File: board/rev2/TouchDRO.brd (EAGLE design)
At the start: 50.8 x 50.8 mm, 26 parts, among them U2 VREG_33, U3 VREG_5

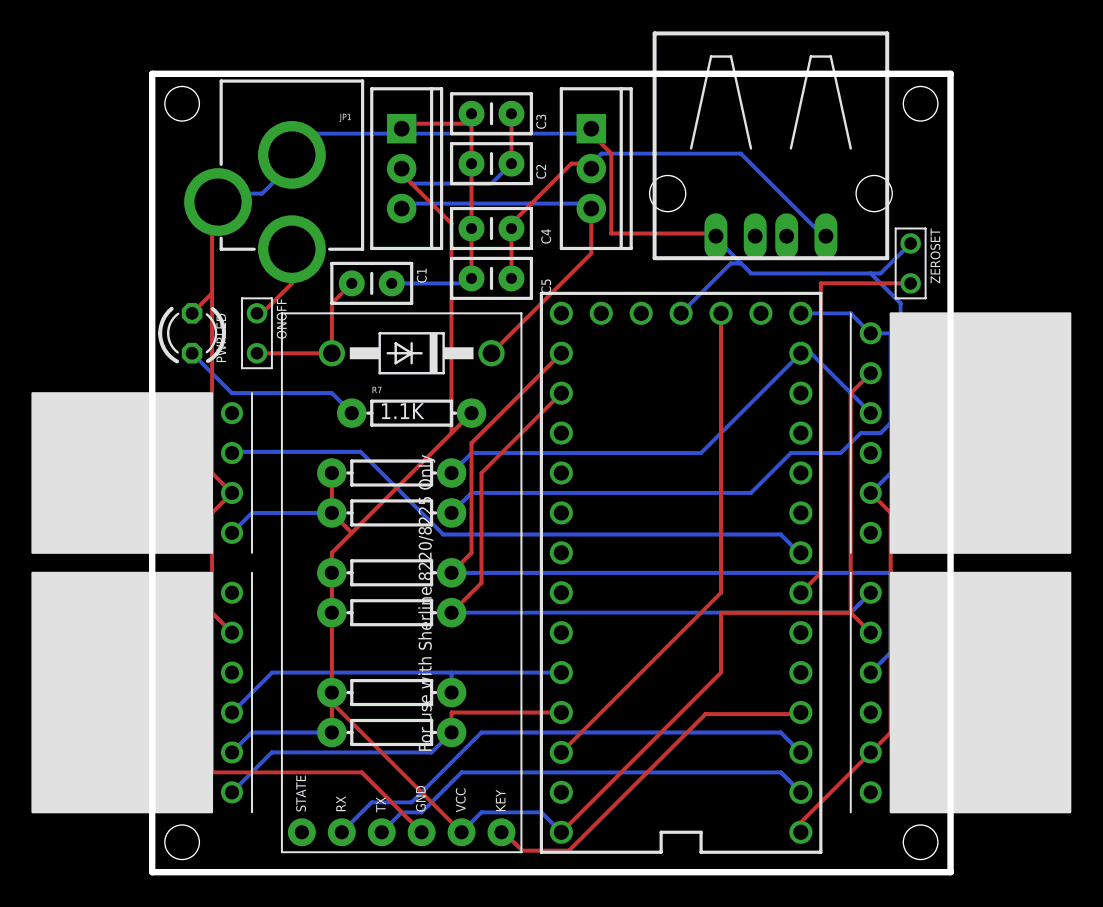
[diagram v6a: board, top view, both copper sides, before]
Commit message: renamed connectors library. update regulators to have PWR signal pin. added Vcc resistor to support sherline encoder. updated TouchDRO sketch to use the new button and frequency libraries, disable bluetooth name set functionality
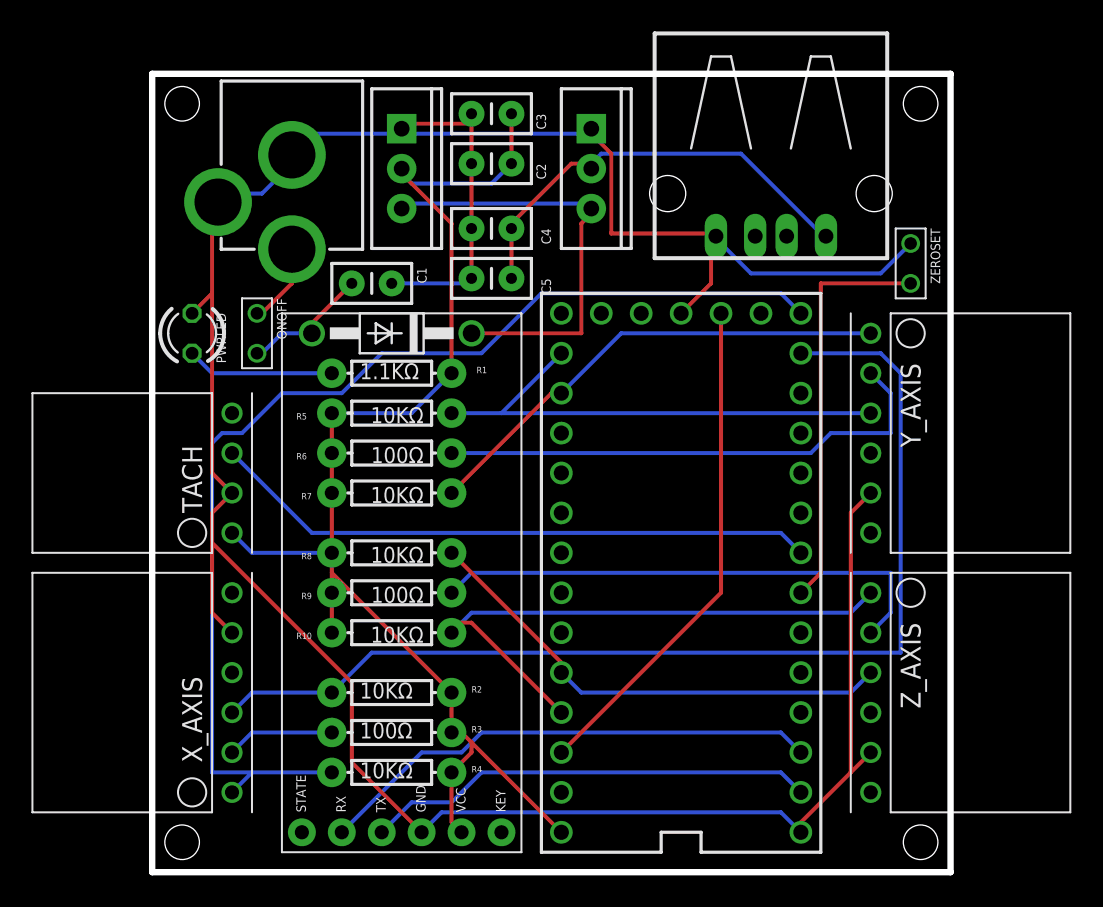
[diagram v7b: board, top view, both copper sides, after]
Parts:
- added R10, R8: 10KΩ, SparkFun-Passives:AXIAL-0.3EZ
- added R9: 100Ω, SparkFun-Passives:AXIAL-0.3EZ
- C1: value 100uF -> 100µF
- C2, C4: value 10uF -> 10µF
- C3, C5: value 0.1uF -> 0.1µF
- R1: value 10K -> 1.1KΩ
- R2, R4, R5: value 10K -> 10KΩ
- R3, R6: value 10K -> 100Ω
- R7: value 1.1K -> 10KΩ
- U$1: value TEENSY_3.2 -> TEENSY
- moved X_AXIS 53.4 mm to (5.08, 5.08), turned to 90 degrees
- moved Z_AXIS 47.8 mm to (45.7, 17.8), turned to 270 degrees
- moved Y_AXIS 21.3 mm to (45.7, 34.3)
- moved R5 17.8 mm to (15.2, 29.2), turned to 180 degrees
- moved R6 17.8 mm to (15.2, 26.7), turned to 180 degrees
- moved R2 11.4 mm to (15.2, 11.4)
- moved R4 10.2 mm to (15.2, 6.35)
- moved R3 10.2 mm to (15.2, 8.89)
- moved R1 6.35 mm to (15.2, 31.8)
- moved R7 5.24 mm to (15.2, 24.1), turned to 180 degrees
- moved D3 1.80 mm to (15.2, 34.3)
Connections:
- removed net KEY: J_BT_BOARD_1.KEY, U$1.2
- new net N$3: R9.P$1, Z_AXIS.P$2
- new net N$5: R6.P$1, Y_AXIS.P$2
- new net N$7: R3.P$1, X_AXIS.P$2
- net +3V3: now also R1.P$2, R10.P$2, R2.P$2, R3.P$2, R4.P$2, R5.P$2, R6.P$2, R8.P$2, R9.P$2; no longer R1.P$1, R2.P$1, R3.P$1, R4.P$1, R5.P$1, R6.P$1, X_AXIS.P$2, Y_AXIS.P$2, Z_AXIS.P$2
- net N$1: now also R1.P$1; no longer R7.P$1
- net X_A: now also R2.P$1; no longer R1.P$2
- net X_B: now also R4.P$1; no longer R2.P$2
- net Y_A: now also R5.P$1; no longer R3.P$2
- net Y_B: now also R7.P$1; no longer R4.P$2
- net Z_A: now also R8.P$1; no longer R5.P$2
- net Z_B: now also R10.P$1; no longer R6.P$2
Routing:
- net +3V3: track 134.6 -> 84.8 mm
- net X_A: track 31.4 -> 68.8 mm
- net N$3: track 0.00 -> 32.8 mm
- net N$5: track 0.00 -> 32.8 mm
- net X_B: track 42.3 -> 72.3 mm
- net KEY: track 23.2 -> 0.00 mm
- net Y_A: track 51.7 -> 32.1 mm
- net Z_B: track 23.8 -> 37.7 mm
- net Y_B: track 44.1 -> 30.9 mm
- net GND: track 176.7 -> 186.6 mm
- net Z_A: track 23.3 -> 31.3 mm
- net N$7: track 0.00 -> 6.88 mm
- net D1: track 24.5 -> 27.9 mm
- net N$1: track 11.7 -> 9.42 mm
- net ONOFF: track 9.73 -> 8.25 mm
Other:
- board text removed: "For use with Sherline 8220/8225 Only"

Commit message: cleaned up connector components. updated images
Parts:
- renumbered U2 to VREG33, U3 to VREG50
